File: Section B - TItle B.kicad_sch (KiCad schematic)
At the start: 0 parts

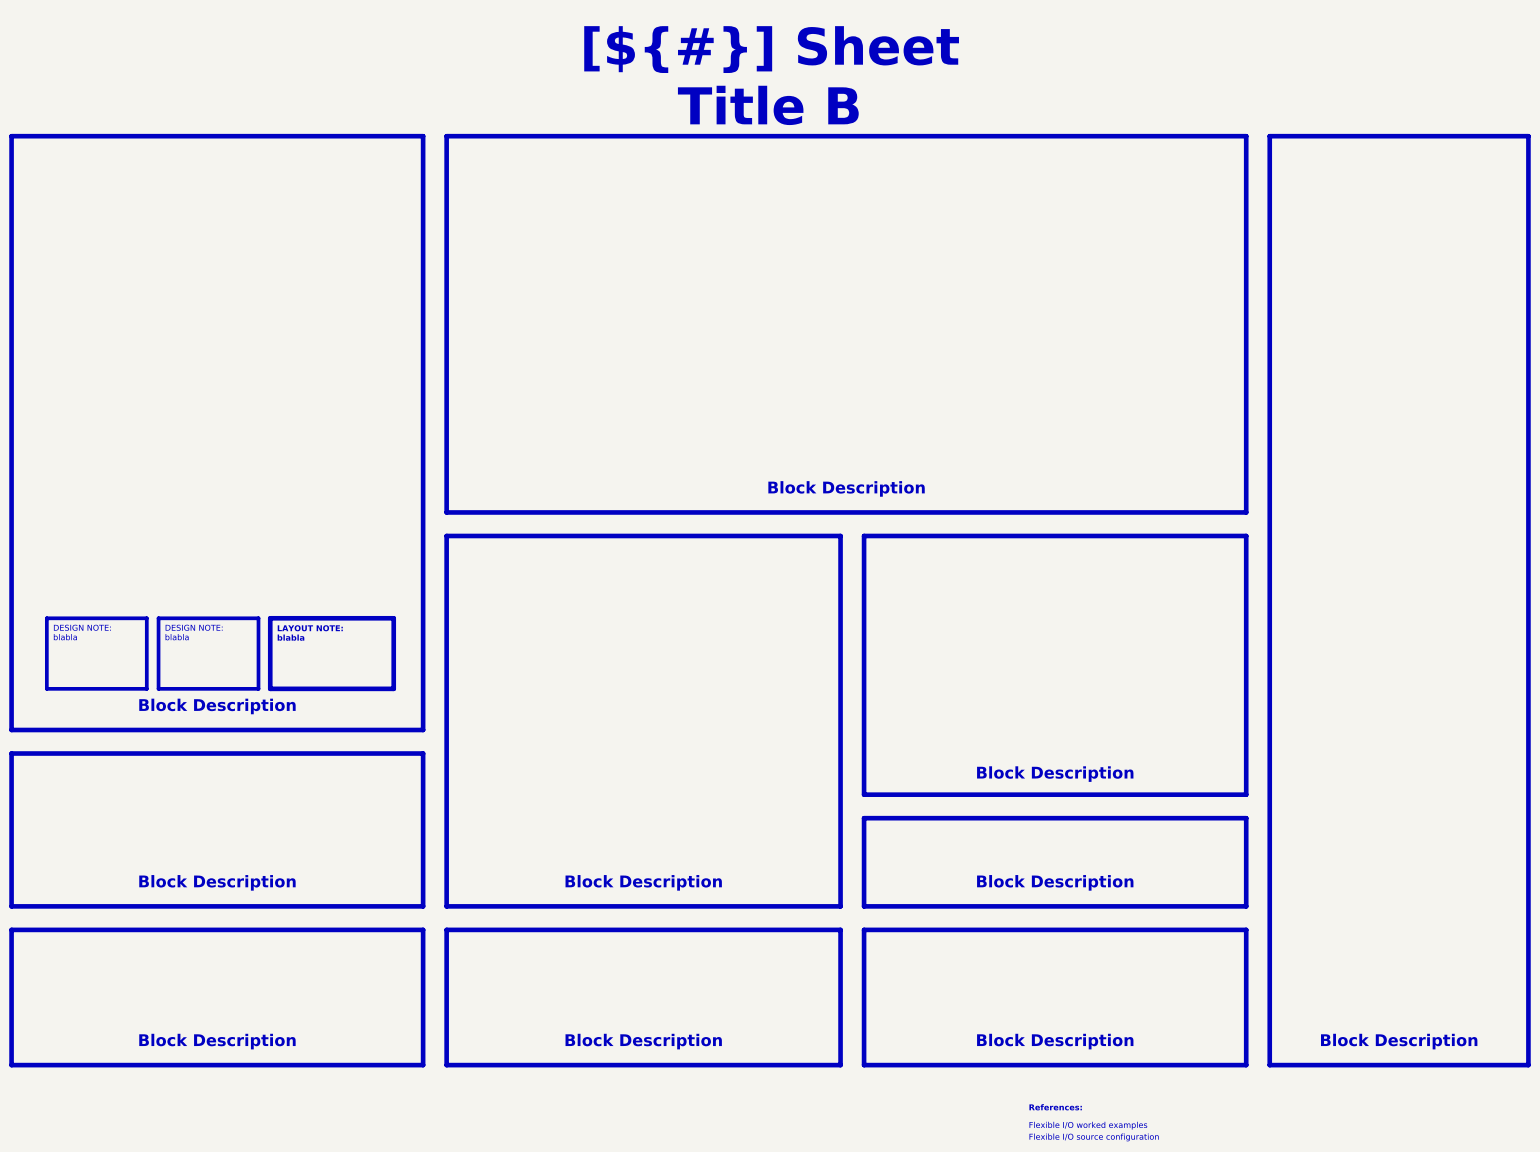
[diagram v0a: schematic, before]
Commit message: [ADD TPS6108]
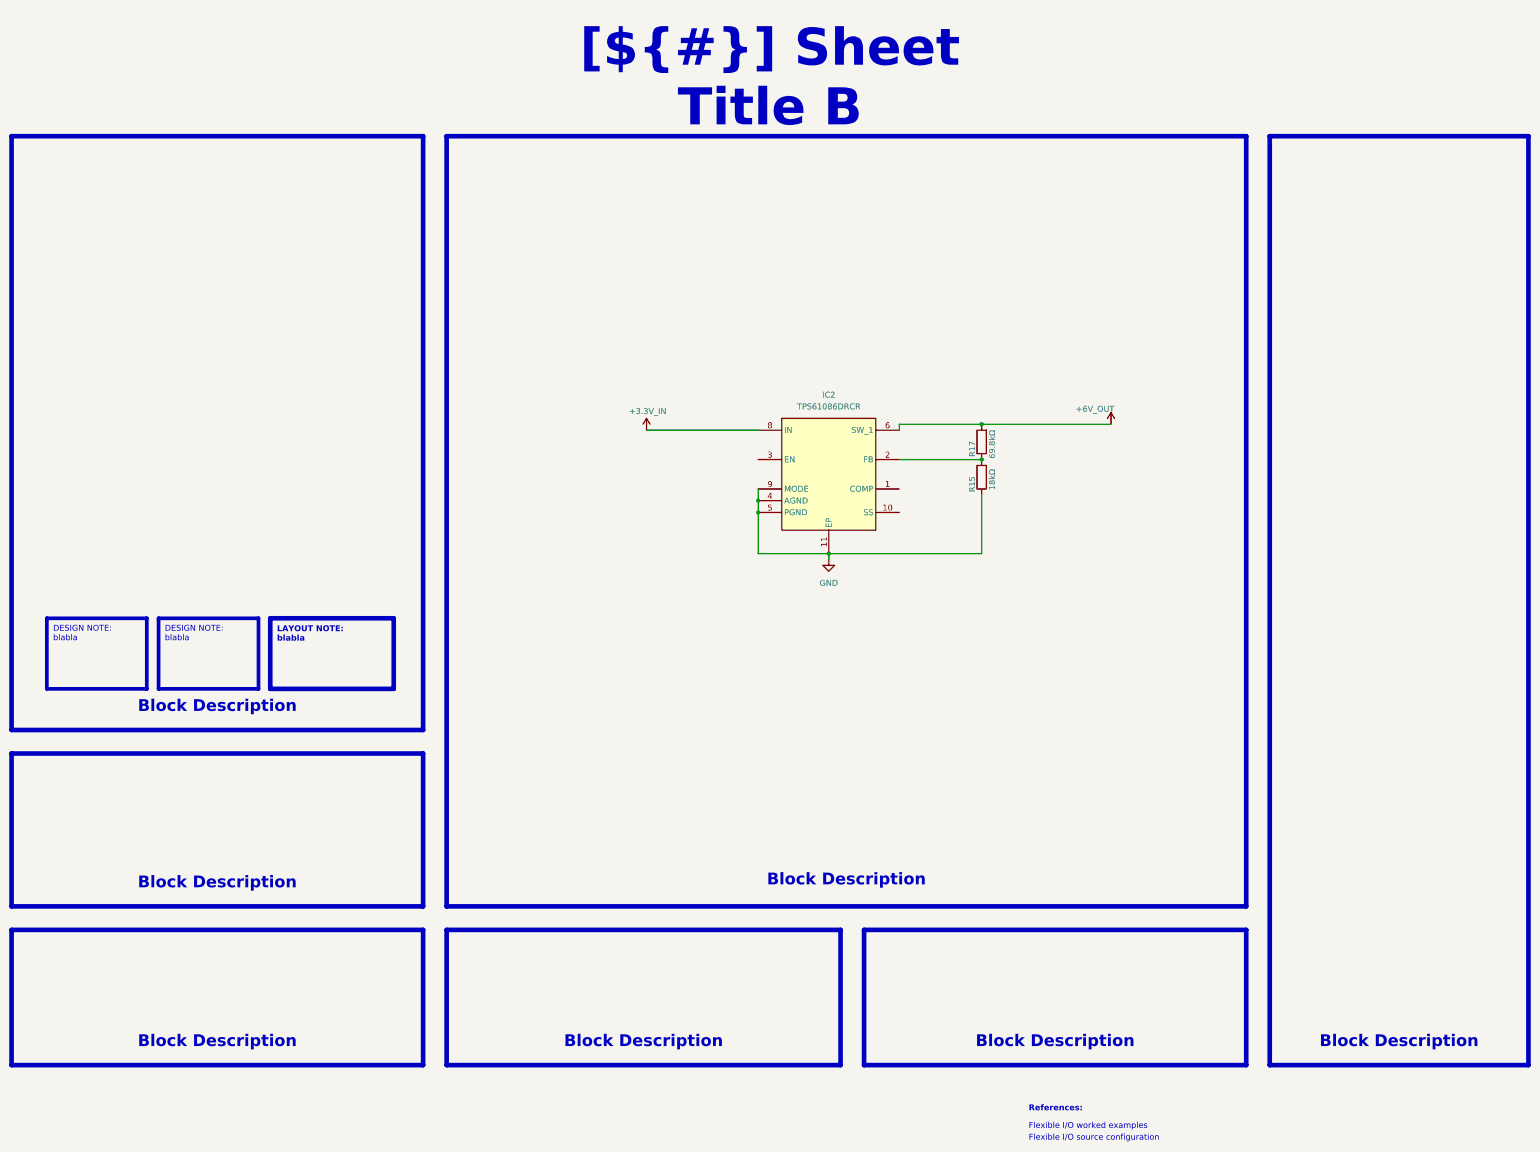
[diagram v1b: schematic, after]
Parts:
- added IC2: TPS61086DRCR, TPS16412DRCR, symbol TPS61086DRCR:TPS61086DRCR
- added R15: 18kΩ, Resistor_SMD:R_0603_1608Metric, symbol Device:R
- added R17: 69.8kΩ, Resistor_SMD:R_0603_1608Metric, symbol Device:R
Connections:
- new net: IC2.2 (FB), R15.2, R17.1
- new net +3.3V_IN: IC2.8 (IN)
- new net +6V_OUT: IC2.6 (SW_1), IC2.7 (SW_2), R17.2
- new net GND: IC2.11 (EP), IC2.12 (EP_2), IC2.13 (EP_3), IC2.14 (EP_4), IC2.15 (EP_5), IC2.4 (AGND), IC2.5 (PGND), IC2.9 (MODE), R15.1
